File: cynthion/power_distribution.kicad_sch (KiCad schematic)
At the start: 80 parts, among them Q1 PMOS, Q10 2PNP, Q11 2NPN, Q12 PMOS, Q13 2PNP, Q14 2PNP, Q15 2PNP, Q2 PMOS, Q3 2NPN, Q4 PMOS, Q5 PMOS, Q6 PMOS, Q7 PMOS, Q8 2NPN, Q9 PMOS, U1 PAC1954

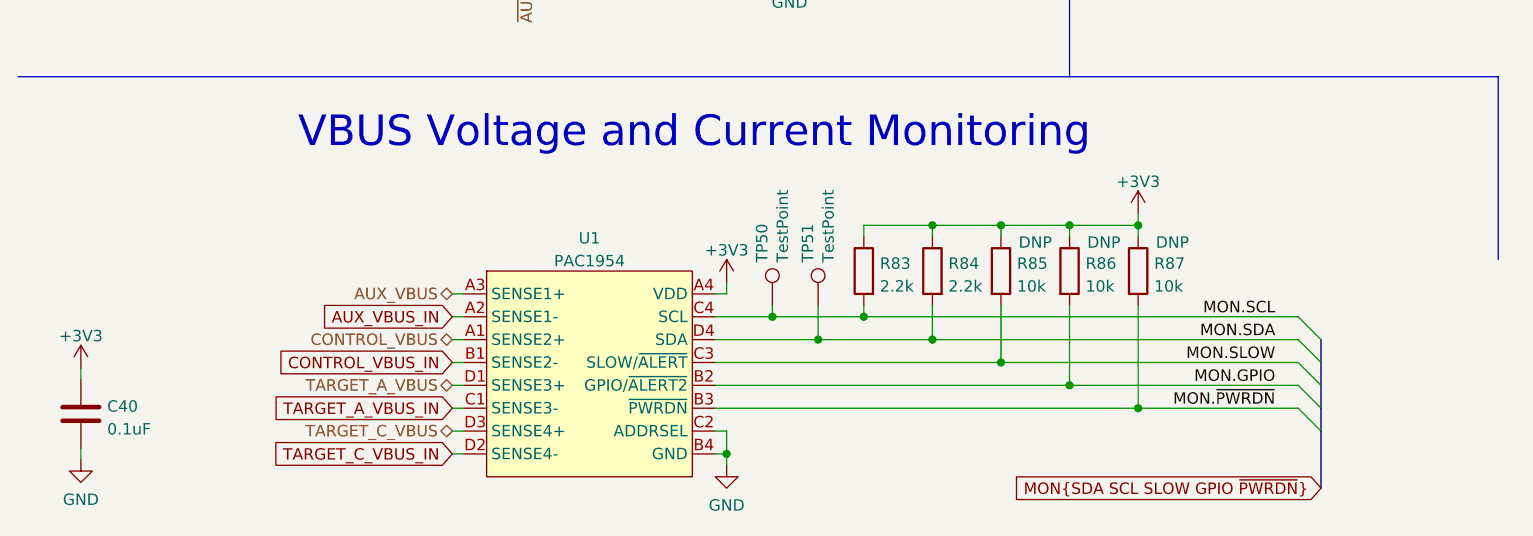
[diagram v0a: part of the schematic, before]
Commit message: hardware: change U1 from WLCSP to VQFN package
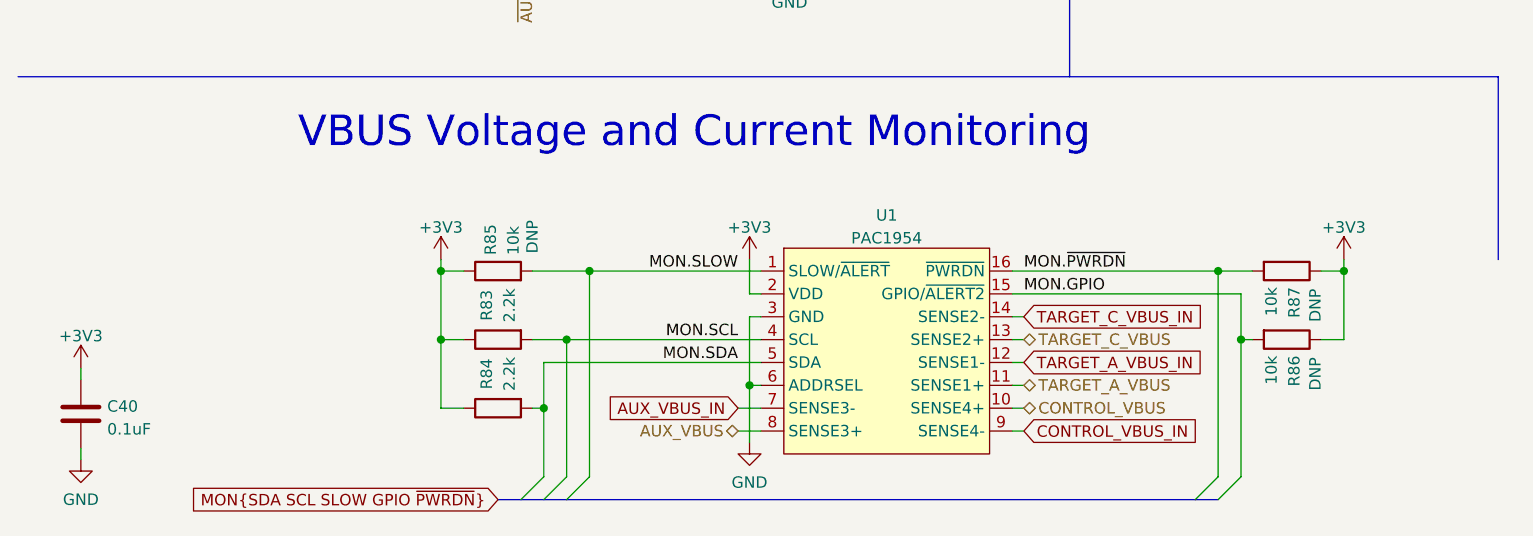
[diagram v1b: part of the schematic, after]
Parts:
- removed TP50, TP51: TestPoint, TestPoint:TestPoint_Pad_D1.0mm, symbol Connector:TestPoint
- U1: footprint luna:WLCSP-16_2.225x2.170mm_Layout4x4_P0.5mm -> Package_DFN_QFN:QFN-16-1EP_3x3mm_P0.5mm_EP1.45x1.45mm; symbol support_hardware:PAC195X-1-WLCSP -> support_hardware:PAC195X-1-VQFN; Part Number PAC1954T-E/J6CX -> PAC1954T-E/4MX
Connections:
- net +3V3: now also U1.2 (VDD); no longer U1.A4 (VDD)
- net AUX_VBUS: now also U1.8 (SENSE3+); no longer U1.A3 (SENSE1+)
- net AUX_VBUS_IN: now also U1.7 (SENSE3-); no longer U1.A2 (SENSE1-)
- net CONTROL_VBUS: now also U1.10 (SENSE4+); no longer U1.A1 (SENSE2+)
- net CONTROL_VBUS_IN: now also U1.9 (SENSE4-); no longer U1.B1 (SENSE2-)
- net GND: now also U1.17 (GND), U1.3 (GND), U1.6 (ADDRSEL); no longer U1.B4 (GND), U1.C2 (ADDRSEL)
- net MON.GPIO: now also U1.15 (GPIO/~{ALERT2}); no longer U1.B2 (GPIO/~{ALERT2})
- net MON.SCL: now also U1.4 (SCL); no longer U1.C4 (SCL)
- net MON.SDA: now also U1.5 (SDA); no longer U1.D4 (SDA)
- net MON.SLOW: now also U1.1 (SLOW/~{ALERT}); no longer U1.C3 (SLOW/~{ALERT})
- net MON.~{PWRDN}: now also U1.16 (~{PWRDN}); no longer U1.B3 (~{PWRDN})
- net TARGET_A_VBUS: now also U1.11 (SENSE1+); no longer U1.D1 (SENSE3+)
- net TARGET_A_VBUS_IN: now also U1.12 (SENSE1-); no longer U1.C1 (SENSE3-)
- net TARGET_C_VBUS: now also U1.13 (SENSE2+); no longer U1.D3 (SENSE4+)
- net TARGET_C_VBUS_IN: now also U1.14 (SENSE2-); no longer U1.D2 (SENSE4-)
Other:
- moved on the sheet: R83, R84, R85, R86, R87, U1
